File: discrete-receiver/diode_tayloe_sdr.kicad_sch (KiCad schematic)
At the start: 9 parts, among them J4 IQ Out, J5 Display Connector, X1 YC24.576MUBCE2O

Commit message: :)
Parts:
- C48: Manufacturer Samsung Electro-Mechanics -> (none); Price 0.009USD -> (none)
- R1, R4: Manufacturer UNI-ROYAL(Uniroyal Elec) -> (none); Price 0.004USD -> (none)
- R34: Manufacturer UNI-ROYAL(Uniroyal Elec) -> (none); Price 0.005USD -> (none)
- USB1: Manufacturer SHOU HAN(首韩) -> (none)
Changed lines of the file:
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@@
-			)
-		)
-		(property "Price" "0.009USD"
-			(at 251.46 134.62 0)
-			(hide yes)
-			(show_name no)
-			(do_not_autoplace no)
-			(effects
-				(font
-					(size 1.27 1.27)
-				)
 			)
 		)
@@
 		)
 		(property "Category" "Capacitors,Multilayer Ceramic Capacitors MLCC - SMD/SMT"
-			(at 251.46 134.62 0)
-			(hide yes)
-			(show_name no)
-			(do_not_autoplace no)
-			(effects
-				(font
-					(size 1.27 1.27)
-				)
-			)
-		)
-		(property "Manufacturer" "Samsung Electro-Mechanics"
 			(at 251.46 134.62 0)
 			(hide yes)
@@
 			)
 		)
-		(property "Price" "0.005USD"
-			(at 251.46 144.78 0)
-			(hide yes)
-			(show_name no)
-			(do_not_autoplace no)
-			(effects
-				(font
-					(size 1.27 1.27)
-				)
-			)
-		)
 		(property "Process" "SMT"
 			(at 251.46 144.78 0)
@@
 		)
 		(property "Category" "Resistors,Chip Resistor - Surface Mount"
-			(at 251.46 144.78 0)
-			(hide yes)
-			(show_name no)
-			(do_not_autoplace no)
-			(effects
-				(font
-					(size 1.27 1.27)
-				)
-			)
-		)
-		(property "Manufacturer" "UNI-ROYAL(Uniroyal Elec)"
 			(at 251.46 144.78 0)
 			(hide yes)
@@
 		)
 		(property "Manufacturer Part" "TYPE-C 16P(073)"
-			(at 29.21 49.53 0)
-			(hide yes)
-			(show_name no)
-			(do_not_autoplace no)
-			(effects
-				(font
-					(size 1.27 1.27)
-				)
-			)
-		)
-		(property "Manufacturer" "SHOU HAN(首韩)"
 			(at 29.21 49.53 0)
 			(hide yes)
@@
 			)
 		)
-		(property "Price" "0.004USD"
-			(at 49.53 41.91 0)
-			(hide yes)
-			(show_name no)
-			(do_not_autoplace no)
-			(effects
-				(font
-					(size 1.27 1.27)
-				)
-			)
-		)
 		(property "Process" "SMT"
 			(at 49.53 41.91 0)
@@
 		)
 		(property "Category" "Resistors,Chip Resistor - Surface Mount"
-			(at 49.53 41.91 0)
-			(hide yes)
-			(show_name no)
-			(do_not_autoplace no)
-			(effects
-				(font
-					(size 1.27 1.27)
-				)
-			)
-		)
-		(property "Manufacturer" "UNI-ROYAL(Uniroyal Elec)"
 			(at 49.53 41.91 0)
 			(hide yes)
@@
 			)
 		)
-		(property "Price" "0.004USD"
-			(at 49.53 39.37 0)
-			(hide yes)
-			(show_name no)
-			(do_not_autoplace no)
-			(effects
-				(font
-					(size 1.27 1.27)
-				)
-			)
-		)
 		(property "Process" "SMT"
 			(at 49.53 39.37 0)
@@
 			(at 49.53 39.37 0)
 			(hide yes)
-			(show_name no)
-			(do_not_autoplace no)
-			(effects
-				(font
-					(size 1.27 1.27)
-				)
-			)
-		)
-		(property "Manufacturer" "UNI-ROYAL(Uniroyal Elec)"
-			(at 49.53 39.37 0)
-			(hide yes)

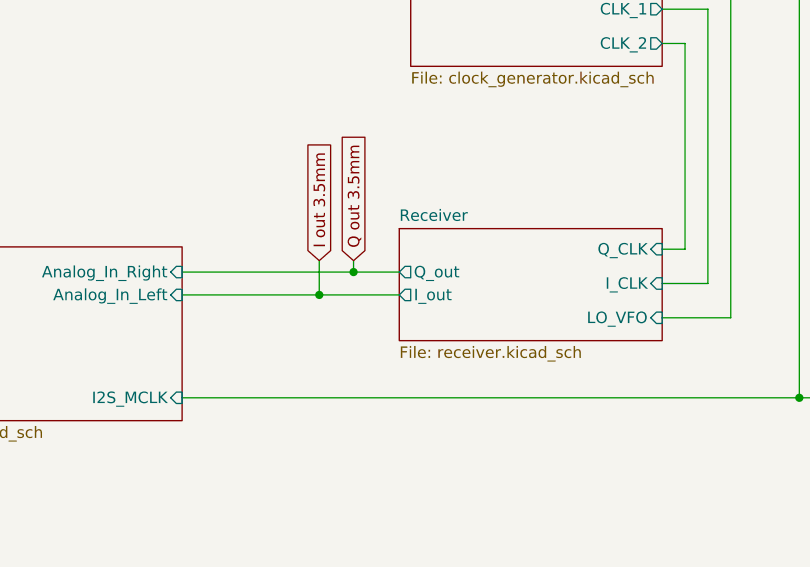
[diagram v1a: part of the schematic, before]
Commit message: Created Tayloe Detector Subsheet
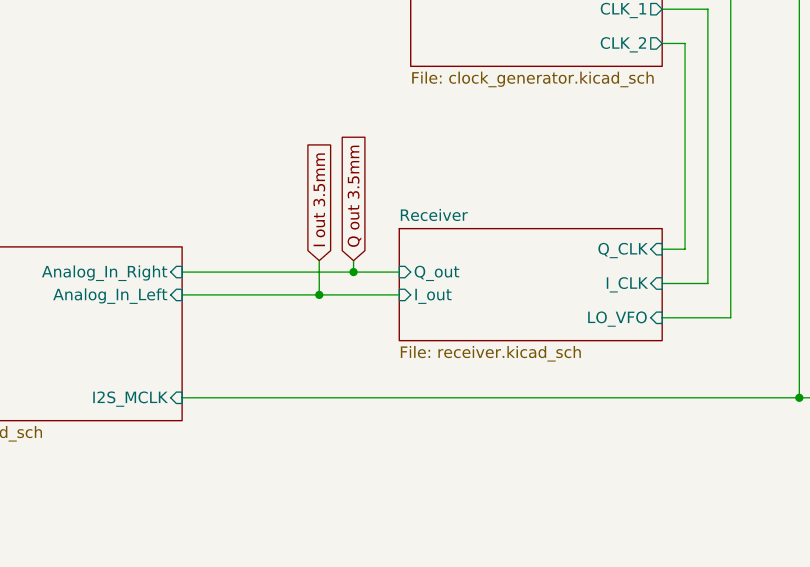
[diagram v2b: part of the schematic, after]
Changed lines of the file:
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@@
 			)
 		)
-		(pin "I_out" output
+		(pin "I_out" input
 			(at 190.5 133.35 180)
 			(effects
@@
 			)
 		)
-		(pin "Q_out" output
+		(pin "Q_out" input
 			(at 190.5 130.81 180)
 			(effects

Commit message: added a footprint to schematic
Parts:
- J5: footprint (none) -> Connector_PinHeader_2.54mm:PinHeader_1x04_P2.54mm_Vertical
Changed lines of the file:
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@@
 		)
 		(instances
-			(project "tayloe_detector"
+			(project "diode_tayloe_sdr"
 				(path "/d18d178d-3f10-4d68-9036-eae71a7d091a"
 					(reference "X1")
@@
 		)
 		(instances
-			(project "tayloe_detector"
+			(project "diode_tayloe_sdr"
 				(path "/d18d178d-3f10-4d68-9036-eae71a7d091a"
 					(reference "#PWR092")
@@
 		)
 		(instances
-			(project "tayloe_detector"
+			(project "diode_tayloe_sdr"
 				(path "/d18d178d-3f10-4d68-9036-eae71a7d091a"
 					(reference "#PWR038")
@@
 		)
 		(instances
-			(project "tayloe_detector"
+			(project "diode_tayloe_sdr"
 				(path "/d18d178d-3f10-4d68-9036-eae71a7d091a"
 					(reference "#PWR081")
@@
 		)
 		(instances
-			(project "tayloe_detector"
+			(project "diode_tayloe_sdr"
 				(path "/d18d178d-3f10-4d68-9036-eae71a7d091a"
 					(reference "#PWR090")
@@
 		)
 		(instances
-			(project "tayloe_detector"
+			(project "diode_tayloe_sdr"
 				(path "/d18d178d-3f10-4d68-9036-eae71a7d091a"
 					(reference "C48")
@@
 		)
 		(instances
-			(project "tayloe_detector"
+			(project "diode_tayloe_sdr"
 				(path "/d18d178d-3f10-4d68-9036-eae71a7d091a"
 					(reference "#PWR082")
@@
 		)
 		(instances
-			(project "tayloe_detector"
+			(project "diode_tayloe_sdr"
 				(path "/d18d178d-3f10-4d68-9036-eae71a7d091a"
 					(reference "#PWR091")
@@
 		)
 		(instances
-			(project "tayloe_detector"
+			(project "diode_tayloe_sdr"
 				(path "/d18d178d-3f10-4d68-9036-eae71a7d091a"
 					(reference "R34")
@@
 		)
 		(instances
-			(project "tayloe_detector"
+			(project "diode_tayloe_sdr"
 				(path "/d18d178d-3f10-4d68-9036-eae71a7d091a"
 					(reference "USB1")
@@
 		)
 		(instances
-			(project "tayloe_detector"
+			(project "diode_tayloe_sdr"
 				(path "/d18d178d-3f10-4d68-9036-eae71a7d091a"
 					(reference "#PWR080")
@@
 			)
 		)
-		(property "Footprint" ""
+		(property "Footprint" "Connector_PinHeader_2.54mm:PinHeader_1x04_P2.54mm_Vertical"
 			(at 39.37 96.52 0)
 			(hide yes)
@@
 		)
 		(instances
-			(project "tayloe_detector"
+			(project "diode_tayloe_sdr"
 				(path "/d18d178d-3f10-4d68-9036-eae71a7d091a"
 					(reference "J5")
@@
 		)
 		(instances
-			(project "tayloe_detector"
+			(project "diode_tayloe_sdr"
 				(path "/d18d178d-3f10-4d68-9036-eae71a7d091a"
 					(reference "JP6")
@@
 		)
 		(instances
-			(project "tayloe_detector"
+			(project "diode_tayloe_sdr"
 				(path "/d18d178d-3f10-4d68-9036-eae71a7d091a"
 					(reference "R4")
@@
 		)
 		(instances
-			(project "tayloe_detector"
+			(project "diode_tayloe_sdr"
 				(path "/d18d178d-3f10-4d68-9036-eae71a7d091a"
 					(reference "R1")
@@
 		)
 		(instances
-			(project "tayloe_detector"
+			(project "diode_tayloe_sdr"
 				(path "/d18d178d-3f10-4d68-9036-eae71a7d091a"
 					(reference "#PWR044")
@@
 		)
 		(instances
-			(project "tayloe_detector"
+			(project "diode_tayloe_sdr"
 				(path "/d18d178d-3f10-4d68-9036-eae71a7d091a"
 					(reference "J4")
@@
 		)
 		(instances
-			(project "tayloe_detector"
+			(project "diode_tayloe_sdr"
 				(path "/d18d178d-3f10-4d68-9036-eae71a7d091a"
 					(page "5")
@@
 		)
 		(instances
-			(project "tayloe_detector"
+			(project "diode_tayloe_sdr"
 				(path "/d18d178d-3f10-4d68-9036-eae71a7d091a"
 					(page "6")
@@
 		)
 		(instances
-			(project "tayloe_detector"
+			(project "diode_tayloe_sdr"
 				(path "/d18d178d-3f10-4d68-9036-eae71a7d091a"
 					(page "4")
@@
 		)
 		(instances
-			(project "tayloe_detector"
+			(project "diode_tayloe_sdr"
 				(path "/d18d178d-3f10-4d68-9036-eae71a7d091a"
 					(page "2")
@@
 		)
 		(instances
-			(project "tayloe_detector"
+			(project "diode_tayloe_sdr"
 				(path "/d18d178d-3f10-4d68-9036-eae71a7d091a"
 					(page "7")
@@
 		)
 		(instances
-			(project "tayloe_detector"
+			(project "diode_tayloe_sdr"
 				(path "/d18d178d-3f10-4d68-9036-eae71a7d091a"
 					(page "3")

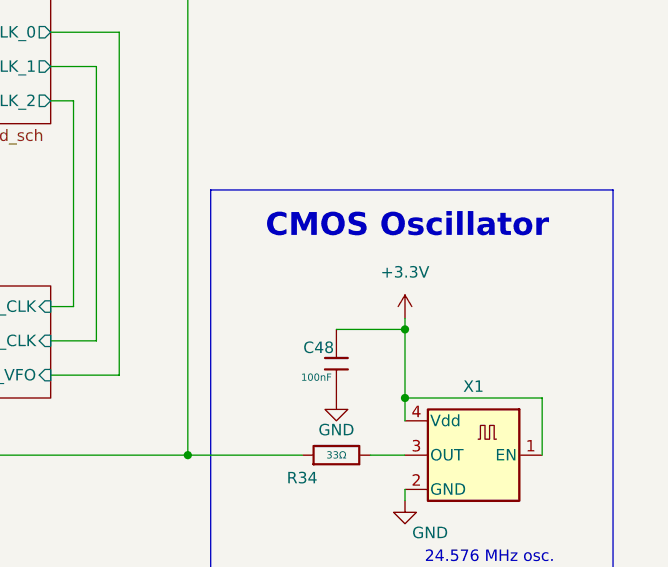
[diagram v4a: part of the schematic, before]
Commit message: Added separate voltage regulators for si5351 and cmos oscillator
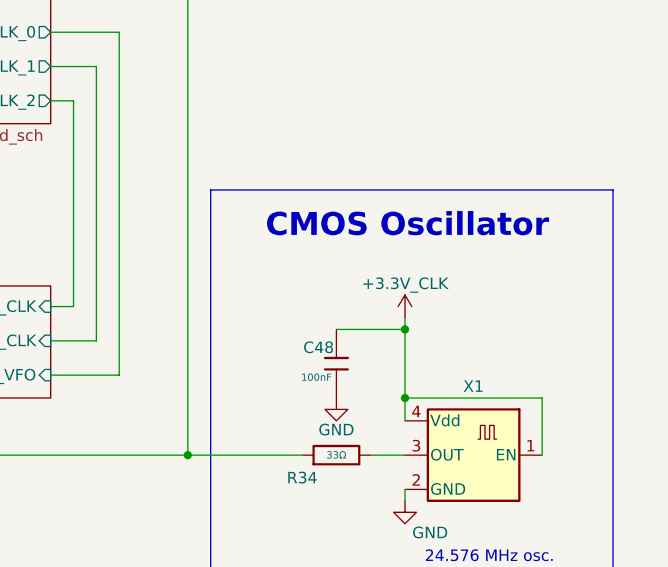
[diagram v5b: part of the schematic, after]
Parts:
- J5: footprint Connector_PinHeader_2.54mm:PinHeader_1x04_P2.54mm_Vertical -> (none)
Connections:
- net +3.3V: no longer C48.1, X1.1 (EN), X1.4 (Vdd)
- new net +3.3V_CLK: C48.1, X1.1 (EN), X1.4 (Vdd)
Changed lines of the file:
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@@
 		)
 		(instances
-			(project "diode_tayloe_sdr"
+			(project "tayloe_detector"
 				(path "/d18d178d-3f10-4d68-9036-eae71a7d091a"
 					(reference "X1")
@@
 		)
 		(instances
-			(project "diode_tayloe_sdr"
+			(project "tayloe_detector"
 				(path "/d18d178d-3f10-4d68-9036-eae71a7d091a"
 					(reference "#PWR092")
@@
 		)
 		(instances
-			(project "diode_tayloe_sdr"
+			(project "tayloe_detector"
 				(path "/d18d178d-3f10-4d68-9036-eae71a7d091a"
 					(reference "#PWR038")
@@
 		)
 		(instances
-			(project "diode_tayloe_sdr"
+			(project "tayloe_detector"
 				(path "/d18d178d-3f10-4d68-9036-eae71a7d091a"
 					(reference "#PWR081")
@@
 		)
 		(instances
-			(project "diode_tayloe_sdr"
+			(project "tayloe_detector"
 				(path "/d18d178d-3f10-4d68-9036-eae71a7d091a"
 					(reference "#PWR090")
@@
 		)
 		(instances
-			(project "diode_tayloe_sdr"
+			(project "tayloe_detector"
 				(path "/d18d178d-3f10-4d68-9036-eae71a7d091a"
 					(reference "C48")
@@
 		)
 		(instances
-			(project "diode_tayloe_sdr"
+			(project "tayloe_detector"
 				(path "/d18d178d-3f10-4d68-9036-eae71a7d091a"
 					(reference "#PWR082")
@@
 		)
 		(instances
-			(project "diode_tayloe_sdr"
+			(project "tayloe_detector"
 				(path "/d18d178d-3f10-4d68-9036-eae71a7d091a"
 					(reference "#PWR091")
@@
 		)
 		(instances
-			(project "diode_tayloe_sdr"
+			(project "tayloe_detector"
 				(path "/d18d178d-3f10-4d68-9036-eae71a7d091a"
 					(reference "R34")
@@
 		)
 		(instances
-			(project "diode_tayloe_sdr"
+			(project "tayloe_detector"
 				(path "/d18d178d-3f10-4d68-9036-eae71a7d091a"
 					(reference "USB1")
@@
 		(lib_id "power:+3.3V")
 		(at 259.08 129.54 0)
-		(mirror y)
 		(unit 1)
 		(body_style 1)
@@
 		(in_pos_files yes)
 		(dnp no)
-		(fields_autoplaced yes)
-		(property "Reference" "#PWR080"
+		(property "Reference" "#PWR0149"
 			(at 259.08 133.35 0)
 			(hide yes)
@@
 			)
 		)
-		(property "Value" "+3.3V"
-			(at 259.08 124.46 0)
+		(property "Value" "+3.3V_CLK"
+			(at 259.08 125.73 0)
 			(show_name no)
 			(do_not_autoplace no)
@@
 			)
 		)
-		(property "Description" ""
+		(property "Description" "Power symbol creates a global label with name \"+3.3V\""
 			(at 259.08 129.54 0)
 			(hide yes)
@@
 		)
 		(instances
-			(project "diode_tayloe_sdr"
+			(project "tayloe_detector"
 				(path "/d18d178d-3f10-4d68-9036-eae71a7d091a"
-					(reference "#PWR080")
+					(reference "#PWR0149")
 					(unit 1)
 				)
@@
 			)
 		)
-		(property "Footprint" "Connector_PinHeader_2.54mm:PinHeader_1x04_P2.54mm_Vertical"
+		(property "Footprint" ""
 			(at 39.37 96.52 0)
 			(hide yes)
@@
 		)
 		(instances
-			(project "diode_tayloe_sdr"
+			(project "tayloe_detector"
 				(path "/d18d178d-3f10-4d68-9036-eae71a7d091a"
 					(reference "J5")
@@
 		)
 		(instances
-			(project "diode_tayloe_sdr"
+			(project "tayloe_detector"
 				(path "/d18d178d-3f10-4d68-9036-eae71a7d091a"
 					(reference "JP6")
@@
 		)
 		(instances
-			(project "diode_tayloe_sdr"
+			(project "tayloe_detector"
 				(path "/d18d178d-3f10-4d68-9036-eae71a7d091a"
 					(reference "R4")
@@
 		)
 		(instances
-			(project "diode_tayloe_sdr"
+			(project "tayloe_detector"
 				(path "/d18d178d-3f10-4d68-9036-eae71a7d091a"
 					(reference "R1")
@@
 		)
 		(instances
-			(project "diode_tayloe_sdr"
+			(project "tayloe_detector"
 				(path "/d18d178d-3f10-4d68-9036-eae71a7d091a"
 					(reference "#PWR044")
@@
 		)
 		(instances
-			(project "diode_tayloe_sdr"
+			(project "tayloe_detector"
 				(path "/d18d178d-3f10-4d68-9036-eae71a7d091a"
 					(reference "J4")
@@
 		)
 		(instances
-			(project "diode_tayloe_sdr"
+			(project "tayloe_detector"
 				(path "/d18d178d-3f10-4d68-9036-eae71a7d091a"
 					(page "5")
@@
 		)
 		(instances
-			(project "diode_tayloe_sdr"
+			(project "tayloe_detector"
 				(path "/d18d178d-3f10-4d68-9036-eae71a7d091a"
 					(page "6")
@@
 		)
 		(instances
-			(project "diode_tayloe_sdr"
+			(project "tayloe_detector"
 				(path "/d18d178d-3f10-4d68-9036-eae71a7d091a"
 					(page "4")
@@
 		)
 		(instances
-			(project "diode_tayloe_sdr"
+			(project "tayloe_detector"
 				(path "/d18d178d-3f10-4d68-9036-eae71a7d091a"
 					(page "2")
@@
 		)
 		(instances
-			(project "diode_tayloe_sdr"
+			(project "tayloe_detector"
 				(path "/d18d178d-3f10-4d68-9036-eae71a7d091a"
 					(page "7")
@@
 		)
 		(instances
-			(project "diode_tayloe_sdr"
+			(project "tayloe_detector"
 				(path "/d18d178d-3f10-4d68-9036-eae71a7d091a"
 					(page "3")

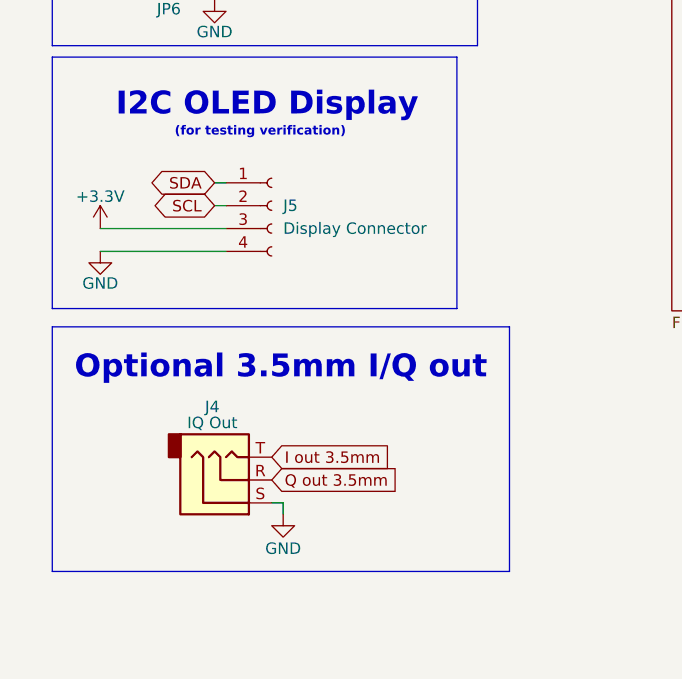
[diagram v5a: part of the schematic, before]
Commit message: all parts now have footprints
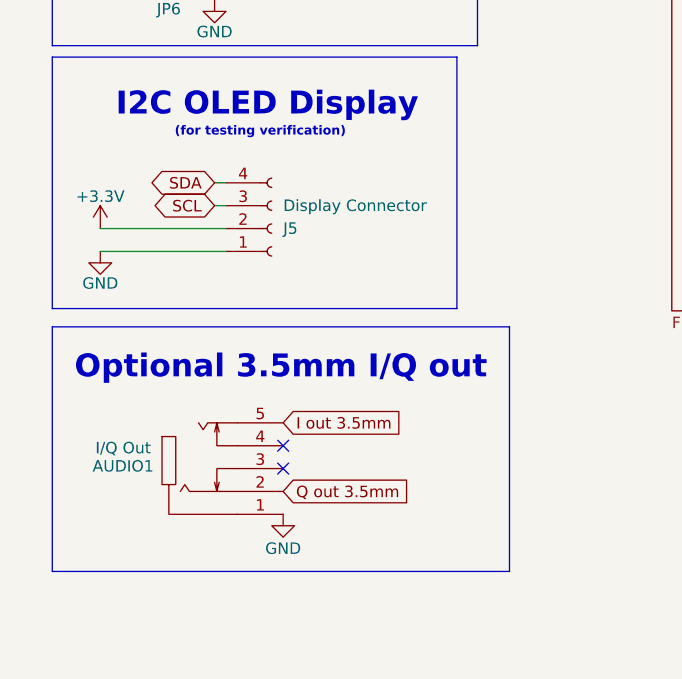
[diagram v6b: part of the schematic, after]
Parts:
- removed J4: IQ Out, symbol Connector_Audio:AudioJack3
- added AUDIO1: I/Q Out, EasyEDA_Lib:AUDIO-TH_PJ-3126-5A, symbol EasyEDA_Lib:PJ-3126-5A
- J5: footprint (none) -> Connector_PinHeader_2.54mm:PinHeader_1x04_P2.54mm_Vertical
- JP6: footprint (none) -> Jumper:SolderJumper-2_P1.3mm_Open_Pad1.0x1.5mm
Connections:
- net +3.3V: now also J5.2 (Pin_2); no longer J5.3 (Pin_3)
- net GND: now also J5.1 (Pin_1), AUDIO1.1; no longer J5.4 (Pin_4)
- net I out 3.5mm: now also AUDIO1.5
- net Q out 3.5mm: now also AUDIO1.2
- net SCL: now also J5.3 (Pin_3); no longer J5.2 (Pin_2)
- net SDA: now also J5.4 (Pin_4); no longer J5.1 (Pin_1)
- no-connect marks 2 -> 4
